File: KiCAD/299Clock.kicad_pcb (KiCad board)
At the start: 2 copper layers, 65 x 80 mm, 30 parts, among them SW1 PEC11R, U1 RPi Pico, U2 RDA5807M, U3 LM386

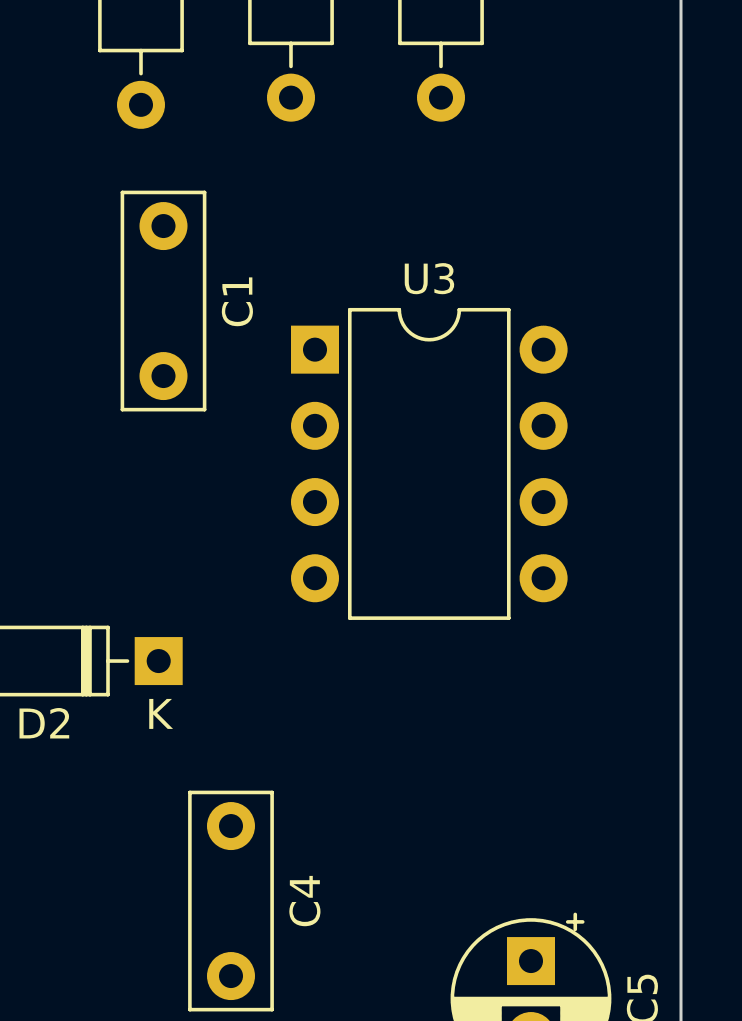
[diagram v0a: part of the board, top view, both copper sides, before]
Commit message: Added test points to PCB
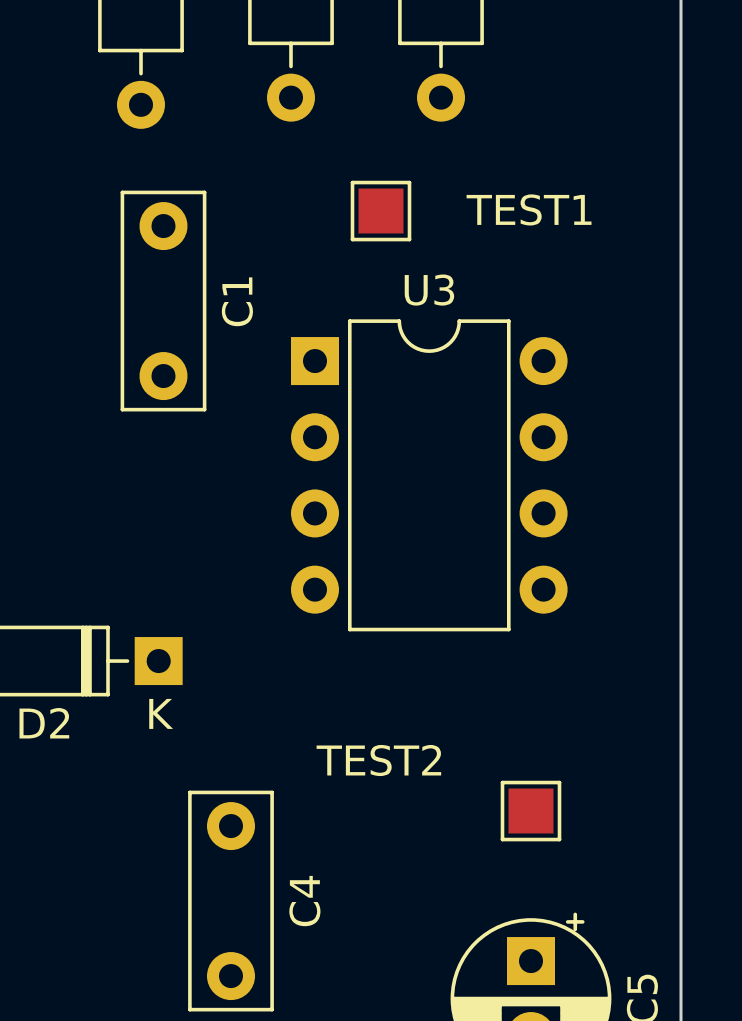
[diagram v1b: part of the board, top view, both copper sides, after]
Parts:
- added TEST1: Conn_01x01, TestPoint:TestPoint_Pad_1.5x1.5mm, F.Cu at (150.0, 75.0)
- added TEST2: Conn_01x01, TestPoint:TestPoint_Pad_1.5x1.5mm, F.Cu at (155.0, 95.0)
- moved U3 0.38 mm to (147.8, 80.0)
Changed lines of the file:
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@@
     )
+  )
+  (footprint "TestPoint:TestPoint_Pad_1.5x1.5mm" (layer "F.Cu")
+    (at 150 75)
+    (descr "SMD rectangular pad as test Point, square 1.5mm side length")
+    (tags "test point SMD pad rectangle square")
+    (property "Sheetfile" "299Clock_v2.kicad_sch")
+    (property "Sheetname" "")
+    (attr exclude_from_pos_files)
+    (fp_text reference "TEST1" (at 5 0) (layer "F.SilkS")
+      (effects (font (size 1 1) (thickness 0.15)))
+    )
+    (fp_text value "Conn_01x01" (at 0 1.75) (layer "F.Fab")
+      (effects (font (size 1 1) (thickness 0.15)))
+    )
+    (fp_text user "${REFERENCE}" (at 0 -1.65) (layer "F.Fab")
+      (effects (font (size 1 1) (thickness 0.15)))
+    )
+    (fp_line (start 0.95 -0.95) (end 0.95 0.95) (layer "F.SilkS") (width 0.12))
+    (fp_line (start 0.95 0.95) (end -0.95 0.95) (layer "F.SilkS") (width 0.12))
+    (fp_line (start -0.95 -0.95) (end 0.95 -0.95) (layer "F.SilkS") (width 0.12))
+    (fp_line (start -0.95 0.95) (end -0.95 -0.95) (layer "F.SilkS") (width 0.12))
+    (fp_line (start -1.25 -1.25) (end -1.25 1.25) (layer "F.CrtYd") (width 0.05))
+    (fp_line (start 1.25 1.25) (end -1.25 1.25) (layer "F.CrtYd") (width 0.05))
+    (fp_line (start -1.25 -1.25) (end 1.25 -1.25) (layer "F.CrtYd") (width 0.05))
+    (fp_line (start 1.25 1.25) (end 1.25 -1.25) (layer "F.CrtYd") (width 0.05))
+    (pad "1" smd rect (at 0 0) (size 1.5 1.5) (layers "F.Cu" "F.Mask")
+      (net 3 "Net-(C1-Pad1)") (pinfunction "Pin_1") (pintype "passive"))
   )
   (footprint "Connector_Wire:SolderWire-0.1sqmm_1x02_P3.6mm_D0.4mm_OD1mm" (layer "F.Cu")
@@
   )
   (footprint "Package_DIP:DIP-8_W7.62mm" (layer "F.Cu")
-    (at 147.8 79.62)
+    (at 147.8 80)
     (descr "8-lead though-hole mounted DIP package, row spacing 7.62 mm (300 mils)")
     (tags "THT DIP DIL PDIP 2.54mm 7.62mm 300mil")
@@
       (net 10 "Net-(C2-Pad2)") (pinfunction "1") (pintype "input"))
   )
+  (footprint "TestPoint:TestPoint_Pad_1.5x1.5mm" (layer "F.Cu")
+    (at 155 95)
+    (descr "SMD rectangular pad as test Point, square 1.5mm side length")
+    (tags "test point SMD pad rectangle square")
+    (property "Sheetfile" "299Clock_v2.kicad_sch")
+    (property "Sheetname" "")
+    (attr exclude_from_pos_files)
+    (fp_text reference "TEST2" (at -5 -1.648) (layer "F.SilkS")
+      (effects (font (size 1 1) (thickness 0.15)))
+    )
+    (fp_text value "Conn_01x01" (at 0 1.75) (layer "F.Fab")
+      (effects (font (size 1 1) (thickness 0.15)))
+    )
+    (fp_text user "${REFERENCE}" (at 0 -1.65) (layer "F.Fab")
+      (effects (font (size 1 1) (thickness 0.15)))
+    )
+    (fp_line (start 0.95 -0.95) (end 0.95 0.95) (layer "F.SilkS") (width 0.12))
+    (fp_line (start 0.95 0.95) (end -0.95 0.95) (layer "F.SilkS") (width 0.12))
+    (fp_line (start -0.95 0.95) (end -0.95 -0.95) (layer "F.SilkS") (width 0.12))
+    (fp_line (start -0.95 -0.95) (end 0.95 -0.95) (layer "F.SilkS") (width 0.12))
+    (fp_line (start -1.25 -1.25) (end 1.25 -1.25) (layer "F.CrtYd") (width 0.05))
+    (fp_line (start 1.25 1.25) (end -1.25 1.25) (layer "F.CrtYd") (width 0.05))
+    (fp_line (start 1.25 1.25) (end 1.25 -1.25) (layer "F.CrtYd") (width 0.05))
+    (fp_line (start -1.25 -1.25) (end -1.25 1.25) (layer "F.CrtYd") (width 0.05))
+    (pad "1" smd rect (at 0 0) (size 1.5 1.5) (layers "F.Cu" "F.Mask")
+      (net 46 "Net-(C4-Pad1)") (pinfunction "Pin_1") (pintype "passive"))
+  )
   (gr_rect (start 95 130) (end 160 50) (layer "Edge.Cuts") (width 0.1) (fill none))

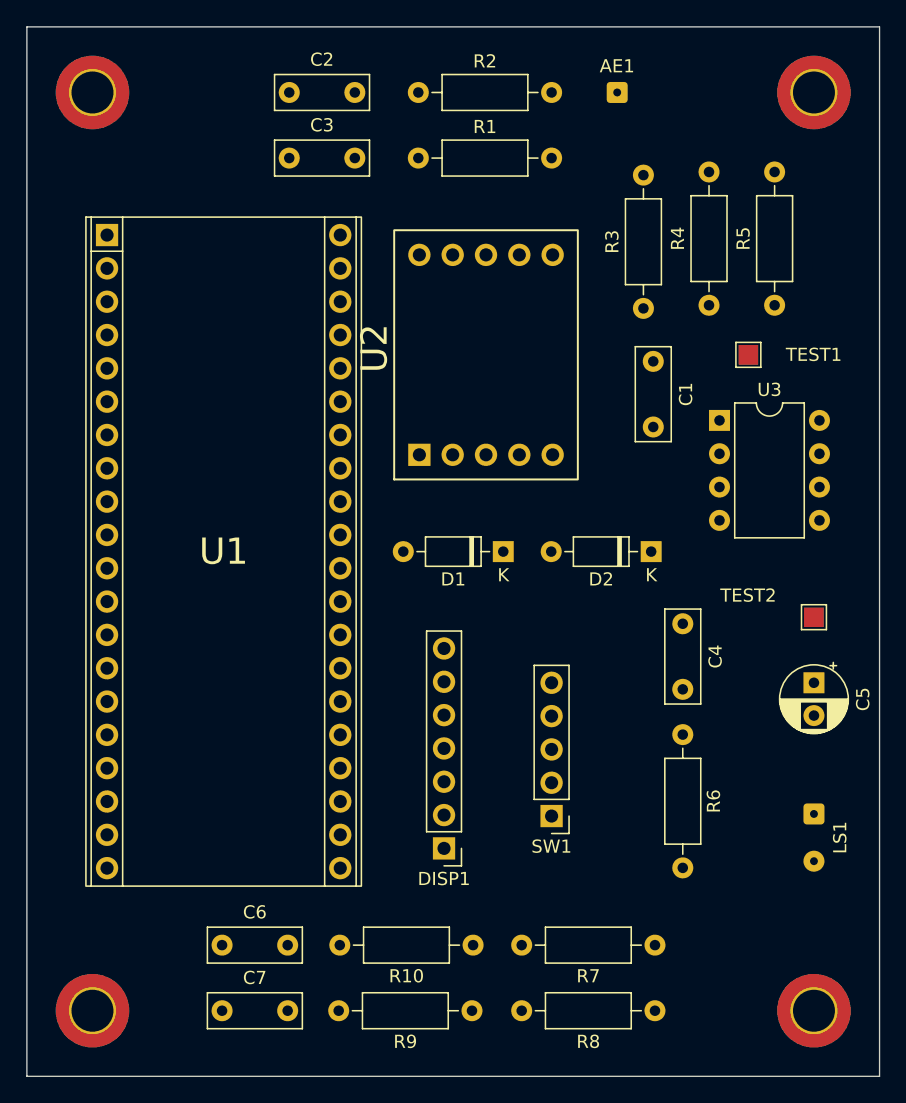
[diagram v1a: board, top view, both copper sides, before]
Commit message: Began adding traces to PCB
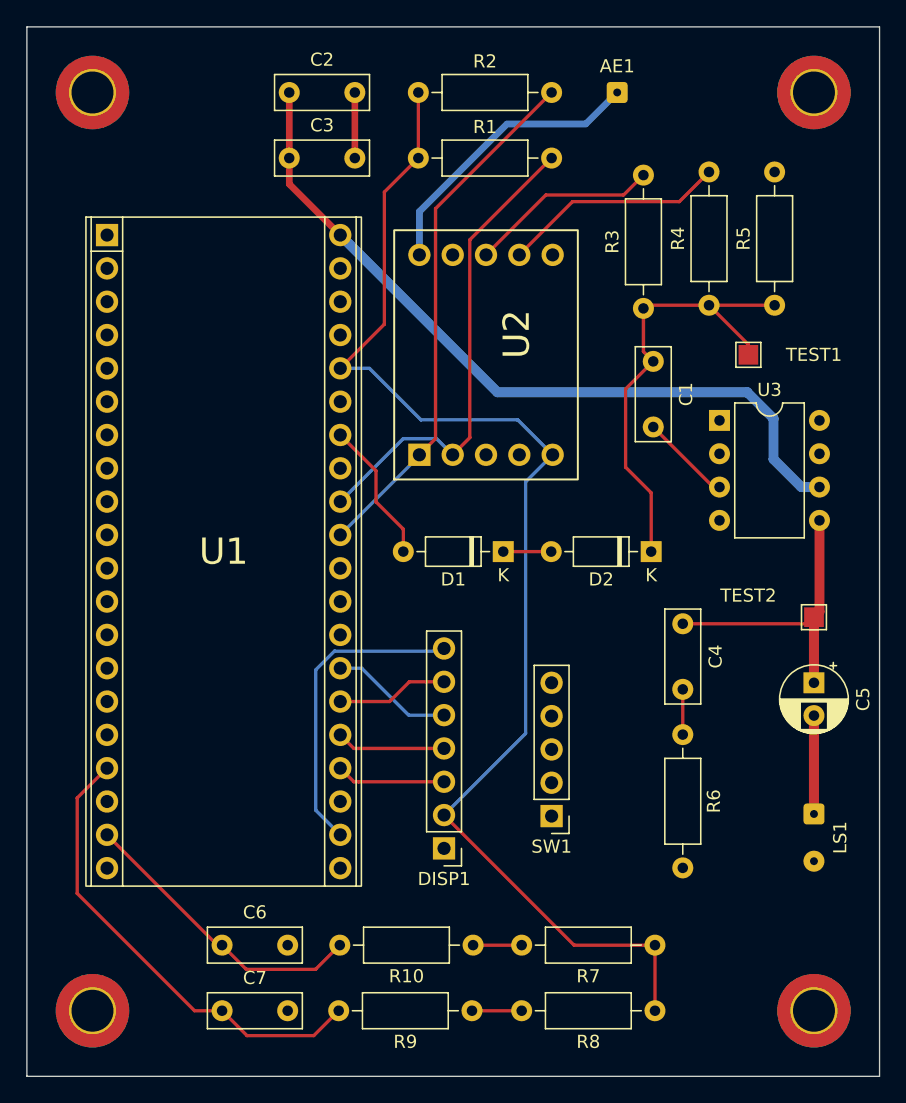
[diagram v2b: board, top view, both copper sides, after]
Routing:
- net Net-(DISP1-Pad2): track 0.00 -> 98.5 mm
- net Net-(C2-Pad1): track 0.00 -> 58.8 mm
- net Net-(R2-Pad2): track 0.00 -> 40.4 mm
- net Net-(R1-Pad2): track 0.00 -> 36.8 mm
- net Net-(C7-Pad1): track 0.00 -> 35.7 mm
- net Net-(C1-Pad1): track 0.00 -> 35.7 mm
- net Net-(DISP1-Pad7): track 0.00 -> 23.8 mm
- net Net-(C4-Pad1): track 0.00 -> 22.8 mm
- net Net-(C6-Pad1): track 0.00 -> 22.8 mm
- net Net-(AE1-Pad1): track 0.00 -> 22.1 mm
- net Net-(R4-Pad2): track 0.00 -> 17.1 mm
- net Net-(R3-Pad2): track 0.00 -> 14.5 mm
- net Net-(D1-Pad2): track 0.00 -> 10.9 mm
- net Net-(DISP1-Pad5): track 0.00 -> 9.39 mm
- net Net-(DISP1-Pad6): track 0.00 -> 8.53 mm
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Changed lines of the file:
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@@
     (property "Sheetname" "")
     (attr through_hole)
-    (fp_text reference "U2" (at 0.5 -8.5 90 unlocked) (layer "F.SilkS")
+    (fp_text reference "U2" (at 1.5686 2.334 90 unlocked) (layer "F.SilkS")
       (effects (font (size 2 2) (thickness 0.25)))
     )
@@
   )
   (gr_rect (start 95 130) (end 160 50) (layer "Edge.Cuts") (width 0.1) (fill none))
+  (segment (start 131.315 90) (end 134.97 90) (width 0.254) (layer "F.Cu") (net 1))
+  (segment (start 123.695 88.2874) (end 121.6152 86.2076) (width 0.254) (layer "F.Cu") (net 2))
+  (segment (start 123.695 90) (end 123.695 88.2874) (width 0.254) (layer "F.Cu") (net 2))
+  (segment (start 121.6152 86.2076) (end 121.6152 83.8352) (width 0.254) (layer "F.Cu") (net 2))
+  (segment (start 121.6152 83.8352) (end 118.89 81.11) (width 0.254) (layer "F.Cu") (net 2))
+  (segment (start 152 71.22) (end 147 71.22) (width 0.254) (layer "F.Cu") (net 3))
+  (segment (start 142.59 85.5162) (end 142.59 90) (width 0.254) (layer "F.Cu") (net 3))
+  (segment (start 142.24 71.22) (end 142 71.46) (width 0.254) (layer "F.Cu") (net 3))
+  (segment (start 147 71.22) (end 150 74.22) (width 0.254) (layer "F.Cu") (net 3))
+  (segment (start 150 74.22) (end 150 75) (width 0.254) (layer "F.Cu") (net 3))
+  (segment (start 147 71.22) (end 142.24 71.22) (width 0.254) (layer "F.Cu") (net 3))
+  (segment (start 142 74.75) (end 142.75 75.5) (width 0.254) (layer "F.Cu") (net 3))
+  (segment (start 142.75 75.5) (end 140.6398 77.6102) (width 0.254) (layer "F.Cu") (net 3))
+  (segment (start 140.6398 77.6102) (end 140.6398 83.566) (width 0.254) (layer "F.Cu") (net 3))
+  (segment (start 140.6398 83.566) (end 142.59 85.5162) (width 0.254) (layer "F.Cu") (net 3))
+  (segment (start 142 71.46) (end 142 74.75) (width 0.254) (layer "F.Cu") (net 3))
+  (segment (start 129.015 120) (end 132.72 120) (width 0.254) (layer "F.Cu") (net 4))
+  (segment (start 128.93 125) (end 132.72 125) (width 0.254) (layer "F.Cu") (net 5))
+  (segment (start 124.84 60) (end 122.2502 62.5898) (width 0.254) (layer "F.Cu") (net 6))
+  (segment (start 122.2502 62.5898) (end 122.2502 72.6698) (width 0.254) (layer "F.Cu") (net 6))
+  (segment (start 124.84 55) (end 124.84 60) (width 0.254) (layer "F.Cu") (net 6))
+  (segment (start 136.715 120) (end 126.8 110.085) (width 0.254) (layer "F.Cu") (net 6))
+  (segment (start 142.88 120) (end 136.715 120) (width 0.254) (layer "F.Cu") (net 6))
+  (segment (start 122.2502 72.6698) (end 118.89 76.03) (width 0.254) (layer "F.Cu") (net 6))
+  (segment (start 142.88 120) (end 142.88 125) (width 0.254) (layer "F.Cu") (net 6))
+  (segment (start 133.0198 84.6802) (end 135.08 82.62) (width 0.254) (layer "B.Cu") (net 6))
+  (segment (start 125.0442 79.9592) (end 132.4192 79.9592) (width 0.254) (layer "B.Cu") (net 6))
+  (segment (start 121.115 76.03) (end 125.0442 79.9592) (width 0.254) (layer "B.Cu") (net 6))
+  (segment (start 133.0198 103.8652) (end 133.0198 84.6802) (width 0.254) (layer "B.Cu") (net 6))
+  (segment (start 126.8 110.085) (end 133.0198 103.8652) (width 0.254) (layer "B.Cu") (net 6))
+  (segment (start 118.89 76.03) (end 121.115 76.03) (width 0.254) (layer "B.Cu") (net 6))
+  (segment (start 132.4192 79.9592) (end 135.08 82.62) (width 0.254) (layer "B.Cu") (net 6))
+  (segment (start 120 55) (end 120 60) (width 0.508) (layer "F.Cu") (net 10))
+  (segment (start 98.8314 108.7886) (end 98.8314 116.0526) (width 0.254) (layer "F.Cu") (net 22))
+  (segment (start 116.8716 126.8984) (end 118.77 125) (width 0.254) (layer "F.Cu") (net 22))
+  (segment (start 111.7784 126.8984) (end 116.8716 126.8984) (width 0.254) (layer "F.Cu") (net 22))
+  (segment (start 107.7788 125) (end 109.88 125) (width 0.254) (layer "F.Cu") (net 22))
+  (segment (start 109.88 125) (end 111.7784 126.8984) (width 0.254) (layer "F.Cu") (net 22))
+  (segment (start 98.8314 116.0526) (end 107.7788 125) (width 0.254) (layer "F.Cu") (net 22))
+  (segment (start 101.11 106.51) (end 98.8314 108.7886) (width 0.254) (layer "F.Cu") (net 22))
+  (segment (start 109.88 120) (end 111.7238 121.8438) (width 0.254) (layer "F.Cu") (net 23))
+  (segment (start 101.11 111.59) (end 109.52 120) (width 0.254) (layer "F.Cu") (net 23))
+  (segment (start 111.7238 121.8438) (end 117.0112 121.8438) (width 0.254) (layer "F.Cu") (net 23))
+  (segment (start 117.0112 121.8438) (end 118.855 120) (width 0.254) (layer "F.Cu") (net 23))
+  (segment (start 109.52 120) (end 109.88 120) (width 0.254) (layer "F.Cu") (net 23))
+  (segment (start 126.604 97.581) (end 126.8 97.385) (width 0.254) (layer "B.Cu") (net 25))
+  (segment (start 117.0178 109.7178) (end 117.0178 99.021303) (width 0.254) (layer "B.Cu") (net 25))
+  (segment (start 118.89 111.59) (end 117.0178 109.7178) (width 0.254) (layer "B.Cu") (net 25))
+  (segment (start 118.458103 97.581) (end 126.604 97.581) (width 0.254) (layer "B.Cu") (net 25))
+  (segment (start 117.0178 99.021303) (end 118.458103 97.581) (width 0.254) (layer "B.Cu") (net 25))
+  (segment (start 120.2944 107.5436) (end 120.2958 107.545) (width 0.254) (layer "F.Cu") (net 26))
+  (segment (start 119.9236 107.5436) (end 120.2944 107.5436) (width 0.254) (layer "F.Cu") (net 26))
+  (segment (start 120.2958 107.545) (end 126.8 107.545) (width 0.254) (layer "F.Cu") (net 26))
+  (segment (start 118.89 106.51) (end 119.9236 107.5436) (width 0.254) (layer "F.Cu") (net 26))
+  (segment (start 118.89 103.97) (end 119.925 105.005) (width 0.254) (layer "F.Cu") (net 27))
+  (segment (start 119.925 105.005) (end 126.8 105.005) (width 0.254) (layer "F.Cu") (net 27))
+  (segment (start 118.89 101.43) (end 122.6488 101.43) (width 0.254) (layer "F.Cu") (net 28))
+  (segment (start 124.1538 99.925) (end 126.8 99.925) (width 0.254) (layer "F.Cu") (net 28))
+  (segment (start 122.6488 101.43) (end 124.1538 99.925) (width 0.254) (layer "F.Cu") (net 28))
+  (segment (start 118.89 98.89) (end 120.5308 98.89) (width 0.254) (layer "B.Cu") (net 29))
+  (segment (start 120.5308 98.89) (end 124.1058 102.465) (width 0.254) (layer "B.Cu") (net 29))
+  (segment (start 124.1058 102.465) (end 126.8 102.465) (width 0.254) (layer "B.Cu") (net 29))
+  (segment (start 126.151 81.389) (end 126.151 63.849) (width 0.254) (layer "F.Cu") (net 32))
+  (segment (start 126.151 63.849) (end 135 55) (width 0.254) (layer "F.Cu") (net 32))
+  (segment (start 124.92 82.62) (end 126.151 81.389) (width 0.254) (layer "F.Cu") (net 32))
+  (segment (start 118.89 88.73) (end 124.92 82.7) (width 0.254) (layer "B.Cu") (net 32))
+  (segment (start 124.92 82.7) (end 124.92 82.62) (width 0.254) (layer "B.Cu") (net 32))
+  (segment (start 127.46 82.62) (end 128.769 81.311) (width 0.254) (layer "F.Cu") (net 33))
+  (segment (start 128.769 81.311) (end 128.769 66.231) (width 0.254) (layer "F.Cu") (net 33))
+  (segment (start 128.769 66.231) (end 135 60) (width 0.254) (layer "F.Cu") (net 33))
+  (segment (start 126.229 81.389) (end 127.46 82.62) (width 0.254) (layer "B.Cu") (net 33))
+  (segment (start 123.691 81.389) (end 126.229 81.389) (width 0.254) (layer "B.Cu") (net 33))
+  (segment (start 118.89 86.19) (end 123.691 81.389) (width 0.254) (layer "B.Cu") (net 33))
+  (segment (start 115 55) (end 115 60) (width 0.508) (layer "F.Cu") (net 37))
+  (segment (start 115 61.98) (end 118.89 65.87) (width 0.508) (layer "F.Cu") (net 37))
+  (segment (start 115 60) (end 115 61.98) (width 0.508) (layer "F.Cu") (net 37))
+  (segment (start 151.9174 82.9564) (end 154.041 85.08) (width 0.762) (layer "B.Cu") (net 37))
+  (segment (start 154.041 85.08) (end 155.42 85.08) (width 0.762) (layer "B.Cu") (net 37))
+  (segment (start 130.871 77.851) (end 149.9108 77.851) (width 0.762) (layer "B.Cu") (net 37))
+  (segment (start 151.9174 79.8576) (end 151.9174 82.9564) (width 0.762) (layer "B.Cu") (net 37))
+  (segment (start 118.89 65.87) (end 130.871 77.851) (width 0.762) (layer "B.Cu") (net 37))
+  (segment (start 149.9108 77.851) (end 151.9174 79.8576) (width 0.762) (layer "B.Cu") (net 37))
+  (segment (start 147 61.06) (end 144.7378 63.3222) (width 0.254) (layer "F.Cu") (net 40))
+  (segment (start 144.7378 63.3222) (end 136.5978 63.3222) (width 0.254) (layer "F.Cu") (net 40))
+  (segment (start 136.5978 63.3222) (end 132.54 67.38) (width 0.254) (layer "F.Cu") (net 40))
+  (segment (start 134.5658 62.8142) (end 130 67.38) (width 0.254) (layer "F.Cu") (net 41))
+  (segment (start 142 61.3) (end 140.4858 62.8142) (width 0.254) (layer "F.Cu") (net 41))
+  (segment (start 140.4858 62.8142) (end 134.5658 62.8142) (width 0.254) (layer "F.Cu") (net 41))
+  (segment (start 137.596 57.404) (end 131.5974 57.404) (width 0.508) (layer "B.Cu") (net 43))
+  (segment (start 124.92 64.0814) (end 124.92 67.38) (width 0.508) (layer "B.Cu") (net 43))
+  (segment (start 131.5974 57.404) (end 124.92 64.0814) (width 0.508) (layer "B.Cu") (net 43))
+  (segment (start 140 55) (end 137.596 57.404) (width 0.508) (layer "B.Cu") (net 43))
+  (segment (start 145 100.5) (end 145 103.95) (width 0.254) (layer "F.Cu") (net 44))
+  (segment (start 147.33 85.08) (end 147.8 85.08) (width 0.254) (layer "F.Cu") (net 45))
+  (segment (start 142.75 80.5) (end 147.33 85.08) (width 0.254) (layer "F.Cu") (net 45))
+  (segment (start 154.5 95.5) (end 155 95) (width 0.254) (layer "F.Cu") (net 46))
+  (segment (start 155.42 87.62) (end 155.42 94.58) (width 0.762) (layer "F.Cu") (net 46))
+  (segment (start 155 100) (end 155 95) (width 0.762) (layer "F.Cu") (net 46))
+  (segment (start 145 95.5) (end 154.5 95.5) (width 0.254) (layer "F.Cu") (net 46))
+  (segment (start 155.42 94.58) (end 155 95) (width 0.762) (layer "F.Cu") (net 46))
+  (segment (start 155 102.5) (end 155 110) (width 0.762) (layer "F.Cu") (net 47))
 )
